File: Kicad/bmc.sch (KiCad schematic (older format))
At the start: 27 parts, among them J1101 Header, J1102 Header, J1103 Conn_01x05, J1104 Double-mini-DIN-6, SW1101 SW_DIP_x01, SW1102 SW_DIP_x01, U1101 STM32F031K6T6

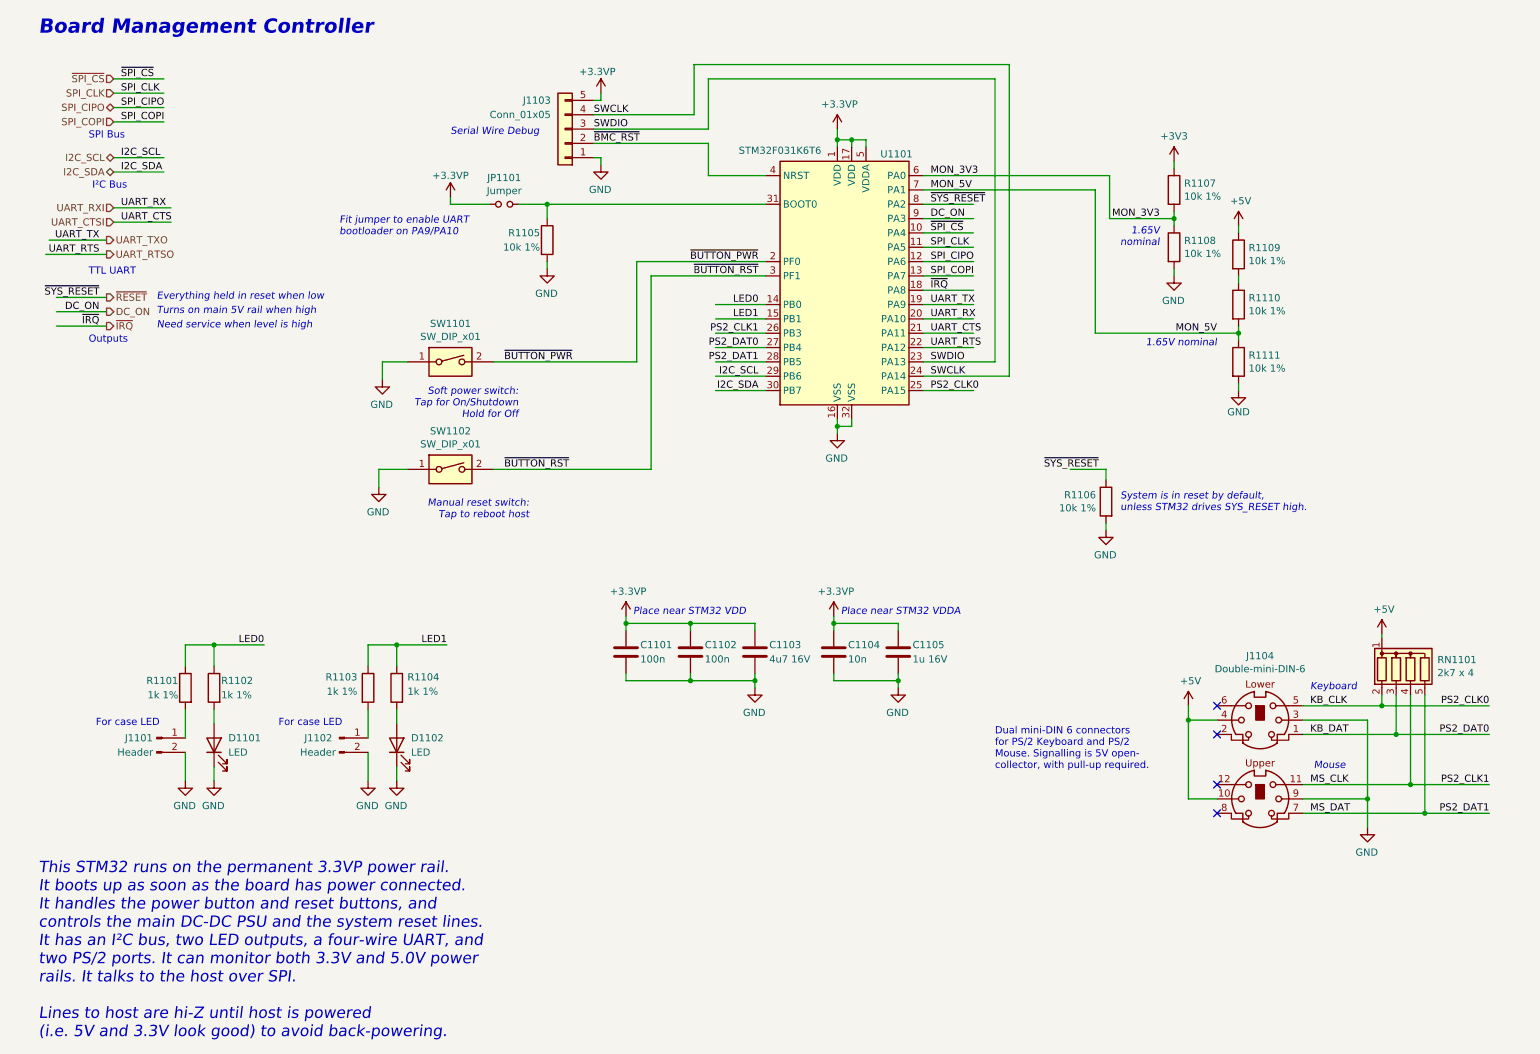
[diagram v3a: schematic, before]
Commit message: BoM and PCB fixes.
* Move tolerances and voltages out of value and into their own fields.
* Fix 5V trace for audio stage.
* Fixup docs.yml so outputs work for JLCPCB.
* Fix JLCPCB part number for 22pF caps.
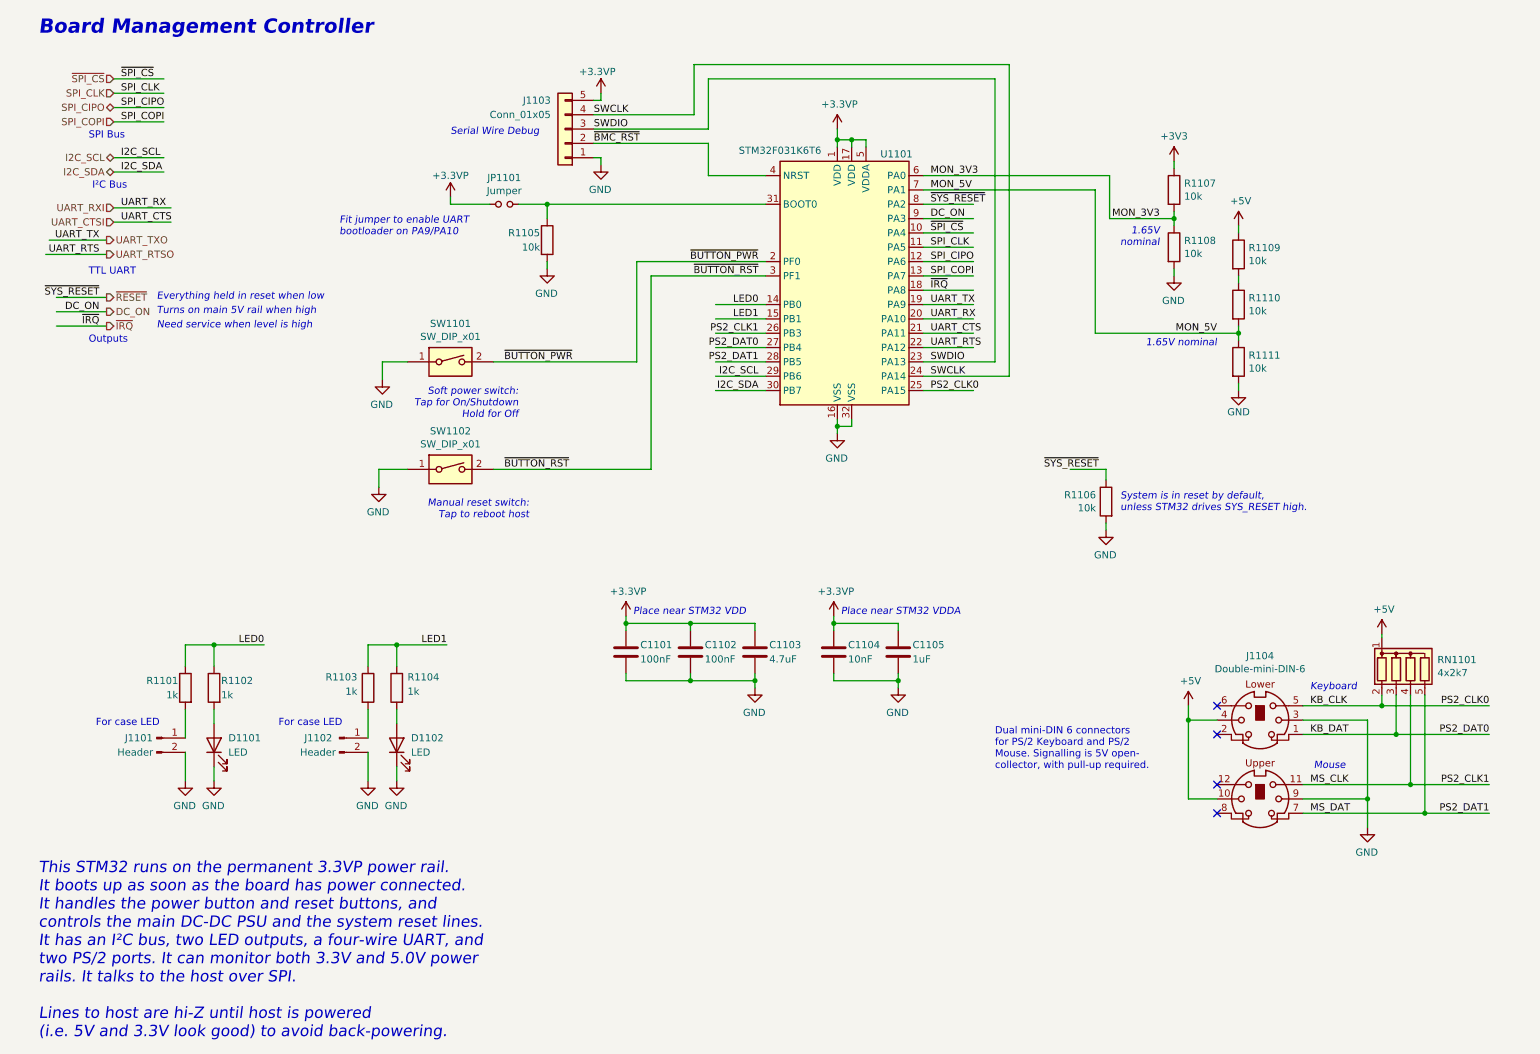
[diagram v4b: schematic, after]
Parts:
- C1101, C1102: value 100n -> 100nF
- C1103: value 4u7 16V -> 4.7uF
- C1104: value 10n -> 10nF
- C1105: value 1u 16V -> 1uF
- R1101, R1102, R1103, R1104: value 1k 1% -> 1k
- R1105, R1106, R1107, R1108, R1109, R1110, R1111: value 10k 1% -> 10k
- RN1101: value 2k7 x 4 -> 4x2k7
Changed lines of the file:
@@
 P 5550 5000
 F 0 "C1103" H 5650 5050 50  0000 L CNN
-F 1 "4u7 16V" H 5650 4950 50  0000 L CNN
+F 1 "4.7uF" H 5650 4950 50  0000 L CNN
 F 2 "Capacitor_SMD:C_0805_2012Metric_Pad1.18x1.45mm_HandSolder" H 5588 4850 50  0001 C CNN
 F 3 "~" H 5550 5000 50  0001 C CNN
@@
 P 5100 5000
 F 0 "C1102" H 5200 5050 50  0000 L CNN
-F 1 "100n" H 5200 4950 50  0000 L CNN
+F 1 "100nF" H 5200 4950 50  0000 L CNN
 F 2 "Capacitor_SMD:C_0805_2012Metric_Pad1.18x1.45mm_HandSolder" H 5138 4850 50  0001 C CNN
 F 3 "~" H 5100 5000 50  0001 C CNN
@@
 P 4650 5000
 F 0 "C1101" H 4750 5050 50  0000 L CNN
-F 1 "100n" H 4750 4950 50  0000 L CNN
+F 1 "100nF" H 4750 4950 50  0000 L CNN
 F 2 "Capacitor_SMD:C_0805_2012Metric_Pad1.18x1.45mm_HandSolder" H 4688 4850 50  0001 C CNN
 F 3 "~" H 4650 5000 50  0001 C CNN
@@
 P 4100 2125
 F 0 "R1105" H 4050 2175 50  0000 R CNN
-F 1 "10k 1%" H 4050 2075 50  0000 R CNN
+F 1 "10k" H 4050 2075 50  0000 R CNN
 F 2 "Resistor_SMD:R_0805_2012Metric_Pad1.20x1.40mm_HandSolder" V 4030 2125 50  0001 C CNN
 F 3 "~" H 4100 2125 50  0001 C CNN
@@
 P 2850 5250
 F 0 "R1103" H 2775 5325 50  0000 R CNN
-F 1 "1k 1%" H 2775 5225 50  0000 R CNN
+F 1 "1k" H 2775 5225 50  0000 R CNN
 F 2 "Resistor_SMD:R_0805_2012Metric_Pad1.20x1.40mm_HandSolder" V 2780 5250 50  0001 C CNN
 F 3 "~" H 2850 5250 50  0001 C CNN
@@
 P 3050 5250
 F 0 "R1104" H 2975 5325 50  0000 R CNN
-F 1 "1k 1%" H 2975 5225 50  0000 R CNN
+F 1 "1k" H 2975 5225 50  0000 R CNN
 F 2 "Resistor_SMD:R_0805_2012Metric_Pad1.20x1.40mm_HandSolder" V 2980 5250 50  0001 C CNN
 F 3 "~" H 3050 5250 50  0001 C CNN
@@
 P 1575 5250
 F 0 "R1101" H 1625 5300 50  0000 L CNN
-F 1 "1k 1%" H 1625 5200 50  0000 L CNN
+F 1 "1k" H 1625 5200 50  0000 L CNN
 F 2 "Resistor_SMD:R_0805_2012Metric_Pad1.20x1.40mm_HandSolder" V 1505 5250 50  0001 C CNN
 F 3 "~" H 1575 5250 50  0001 C CNN
@@
 P 1775 5250
 F 0 "R1102" H 1725 5300 50  0000 R CNN
-F 1 "1k 1%" H 1725 5200 50  0000 R CNN
+F 1 "1k" H 1725 5200 50  0000 R CNN
 F 2 "Resistor_SMD:R_0805_2012Metric_Pad1.20x1.40mm_HandSolder" V 1705 5250 50  0001 C CNN
 F 3 "~" H 1775 5250 50  0001 C CNN
@@
 P 10125 5100
 F 0 "RN1101" H 10313 5146 50  0000 L CNN
-F 1 "2k7 x 4" H 10313 5055 50  0000 L CNN
+F 1 "4x2k7" H 10313 5055 50  0000 L CNN
 F 2 "Resistor_THT:R_Array_SIP5" V 10400 5100 50  0001 C CNN
 F 3 "http://www.vishay.com/docs/31509/csc.pdf" H 10125 5100 50  0001 C CNN
@@
 P 6550 5000
 F 0 "C1105" H 6650 5050 50  0000 L CNN
-F 1 "1u 16V" H 6650 4950 50  0000 L CNN
+F 1 "1uF" H 6650 4950 50  0000 L CNN
 F 2 "Capacitor_SMD:C_0805_2012Metric_Pad1.18x1.45mm_HandSolder" H 6588 4850 50  0001 C CNN
 F 3 "~" H 6550 5000 50  0001 C CNN
@@
 P 6100 5000
 F 0 "C1104" H 6200 5050 50  0000 L CNN
-F 1 "10n" H 6200 4950 50  0000 L CNN
+F 1 "10nF" H 6200 4950 50  0000 L CNN
 F 2 "Capacitor_SMD:C_0805_2012Metric_Pad1.18x1.45mm_HandSolder" H 6138 4850 50  0001 C CNN
 F 3 "~" H 6100 5000 50  0001 C CNN
@@
 P 8925 2975
 F 0 "R1111" H 8995 3021 50  0000 L CNN
-F 1 "10k 1%" H 8995 2930 50  0000 L CNN
+F 1 "10k" H 8995 2930 50  0000 L CNN
 F 2 "Resistor_SMD:R_0805_2012Metric_Pad1.20x1.40mm_HandSolder" V 8855 2975 50  0001 C CNN
 F 3 "~" H 8925 2975 50  0001 C CNN
@@
 P 8925 2575
 F 0 "R1110" H 8995 2621 50  0000 L CNN
-F 1 "10k 1%" H 8995 2530 50  0000 L CNN
+F 1 "10k" H 8995 2530 50  0000 L CNN
 F 2 "Resistor_SMD:R_0805_2012Metric_Pad1.20x1.40mm_HandSolder" V 8855 2575 50  0001 C CNN
 F 3 "~" H 8925 2575 50  0001 C CNN
@@
 P 8925 2225
 F 0 "R1109" H 8995 2271 50  0000 L CNN
-F 1 "10k 1%" H 8995 2180 50  0000 L CNN
+F 1 "10k" H 8995 2180 50  0000 L CNN
 F 2 "Resistor_SMD:R_0805_2012Metric_Pad1.20x1.40mm_HandSolder" V 8855 2225 50  0001 C CNN
 F 3 "~" H 8925 2225 50  0001 C CNN
@@
 P 8475 2175
 F 0 "R1108" H 8545 2221 50  0000 L CNN
-F 1 "10k 1%" H 8545 2130 50  0000 L CNN
+F 1 "10k" H 8545 2130 50  0000 L CNN
 F 2 "Resistor_SMD:R_0805_2012Metric_Pad1.20x1.40mm_HandSolder" V 8405 2175 50  0001 C CNN
 F 3 "~" H 8475 2175 50  0001 C CNN
@@
 P 8475 1775
 F 0 "R1107" H 8545 1821 50  0000 L CNN
-F 1 "10k 1%" H 8545 1730 50  0000 L CNN
+F 1 "10k" H 8545 1730 50  0000 L CNN
 F 2 "Resistor_SMD:R_0805_2012Metric_Pad1.20x1.40mm_HandSolder" V 8405 1775 50  0001 C CNN
 F 3 "~" H 8475 1775 50  0001 C CNN
@@
 P 8000 3950
 F 0 "R1106" H 8070 3996 50  0000 L CNN
-F 1 "10k 1%" H 8070 3905 50  0000 L CNN
+F 1 "10k" H 8070 3905 50  0000 L CNN
 F 2 "Resistor_SMD:R_0805_2012Metric_Pad1.20x1.40mm_HandSolder" V 7930 3950 50  0001 C CNN
 F 3 "~" H 8000 3950 50  0001 C CNN

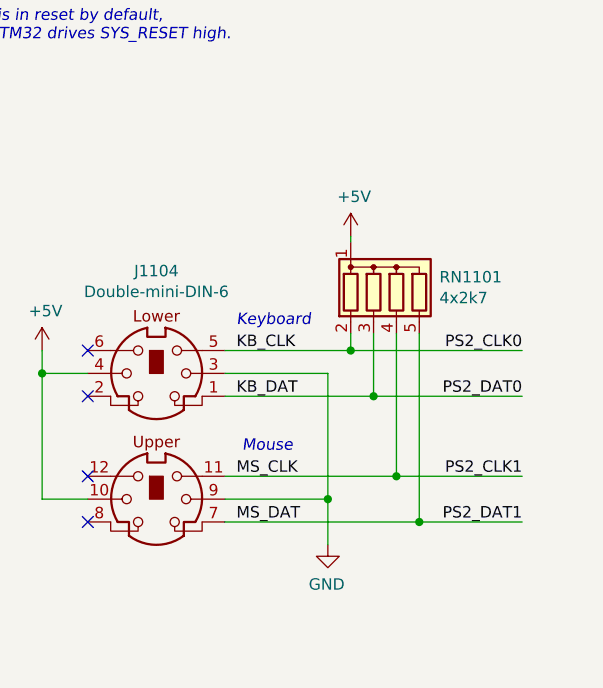
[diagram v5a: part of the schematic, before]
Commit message: Remove PS/2 SIP array and fix DC jack value. (#26)
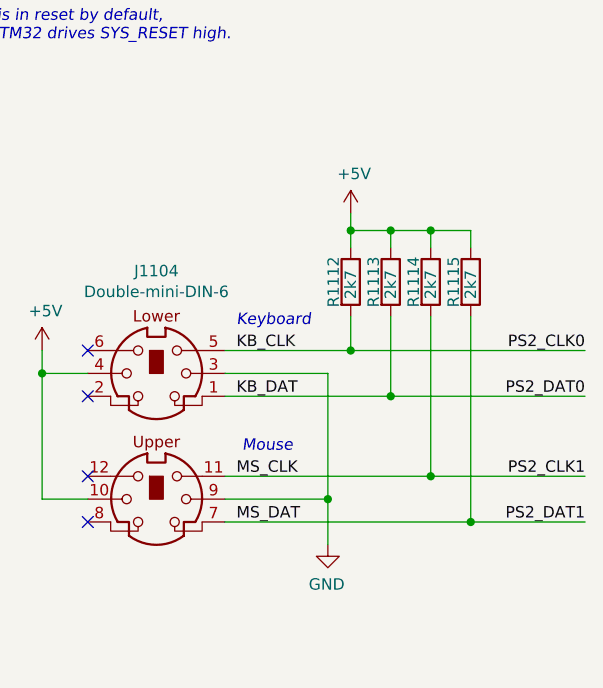
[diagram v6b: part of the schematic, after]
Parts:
- removed RN1101: 4x2k7, Resistor_THT:R_Array_SIP5, symbol Device:R_Network04
- added R1112, R1113, R1114, R1115: 2k7, Resistor_SMD:R_0805_2012Metric_Pad1.20x1.40mm_HandSolder, symbol Device:R
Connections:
- wire segments 150 -> 157
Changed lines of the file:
@@
 	1    0    0    -1
 $EndComp
-Text Label 10675 5375 2    50   ~ 0
+Text Label 10950 5375 2    50   ~ 0
 PS2_CLK0
-Text Label 10675 5575 2    50   ~ 0
+Text Label 10950 5575 2    50   ~ 0
 PS2_DAT0
-Text Label 10675 5925 2    50   ~ 0
+Text Label 10950 5925 2    50   ~ 0
 PS2_CLK1
-Text Label 10675 6125 2    50   ~ 0
+Text Label 10950 6125 2    50   ~ 0
 PS2_DAT1
 Text Notes 9425 5275 0    50   Italic 0
@@
 Mouse
 Wire Wire Line
-	9925 5375 9925 5300
-Wire Wire Line
 	9375 5375 9925 5375
 Wire Wire Line
-	10025 5575 10025 5300
-Wire Wire Line
-	9375 5575 10025 5575
-Wire Wire Line
-	10125 5925 10125 5300
-Wire Wire Line
-	9375 5925 10125 5925
-Wire Wire Line
-	10225 6125 10225 5300
-Wire Wire Line
-	9375 6125 10225 6125
+	9375 5575 10100 5575
+Wire Wire Line
+	9375 5925 10275 5925
+Wire Wire Line
+	9375 6125 10450 6125
 $Comp
 L power:+5V #PWR01124
 U 1 1 6031C569
-P 9925 4875
-F 0 "#PWR01124" H 9925 4725 50  0001 C CNN
-F 1 "+5V" H 9940 5048 50  0000 C CNN
-F 2 "" H 9925 4875 50  0001 C CNN
-F 3 "" H 9925 4875 50  0001 C CNN
-	1    9925 4875
-	1    0    0    -1
-$EndComp
-Wire Wire Line
-	9925 4875 9925 4900
+P 9925 4775
+F 0 "#PWR01124" H 9925 4625 50  0001 C CNN
+F 1 "+5V" H 9940 4948 50  0000 C CNN
+F 2 "" H 9925 4775 50  0001 C CNN
+F 3 "" H 9925 4775 50  0001 C CNN
+	1    9925 4775
+	1    0    0    -1
+$EndComp
 Text Label 5575 2875 2    50   ~ 0
 PS2_DAT0
@@
 	3425 1875 3700 1875
 Wire Wire Line
-	9925 5375 10675 5375
+	9925 5375 10950 5375
 Connection ~ 9925 5375
 Wire Wire Line
-	10025 5575 10675 5575
-Connection ~ 10025 5575
-Wire Wire Line
-	10125 5925 10675 5925
-Connection ~ 10125 5925
-Wire Wire Line
-	10225 6125 10675 6125
-Connection ~ 10225 6125
+	10100 5575 10950 5575
+Connection ~ 10100 5575
+Wire Wire Line
+	10275 5925 10950 5925
+Connection ~ 10275 5925
+Wire Wire Line
+	10450 6125 10950 6125
+Connection ~ 10450 6125
 Text Label 9425 5375 0    50   ~ 0
 KB_CLK
@@
 	1    0    0    -1
 $EndComp
-$Comp
-L Device:R_Network04 RN1101
-U 1 1 60303C59
-P 10125 5100
-F 0 "RN1101" H 10313 5146 50  0000 L CNN
-F 1 "4x2k7" H 10313 5055 50  0000 L CNN
-F 2 "Resistor_THT:R_Array_SIP5" V 10400 5100 50  0001 C CNN
-F 3 "http://www.vishay.com/docs/31509/csc.pdf" H 10125 5100 50  0001 C CNN
-F 4 "0" H 10125 5100 50  0001 C CNN "DNP"
-F 5 "4605X-101-272LF-ND" H 10125 5100 50  0001 C CNN "Digikey"
-F 6 "4605X-101-272LF" H 10125 5100 50  0001 C CNN "MPN"
-F 7 "Bourns" H 10125 5100 50  0001 C CNN "Manufacturer"
-F 8 "652-4605X-1LF-2.7K" H 10125 5100 50  0001 C CNN "Mouser"
-F 9 "~" H 10125 5100 50  0001 C CNN "LCSC Part#"
-	1    10125 5100
-	1    0    0    -1
-$EndComp
 Wire Wire Line
 	4725 2975 4725 2275
@@
 Text Notes 550  7700 0    79   Italic 0
 This STM32 runs on the permanent 3.3VP power rail.\nIt boots up as soon as the board has power connected.\nIt handles the power button and reset buttons, and\ncontrols the main DC-DC PSU and the system reset lines.\nIt has an I²C bus, two LED outputs, a four-wire UART, and\ntwo PS/2 ports. It can monitor both 3.3V and 5.0V power\nrails. It talks to the host over SPI.\n\nLines to host are hi-Z until host is powered\n(i.e. 5V and 3.3V look good) to avoid back-powering.
+$Comp
+L Device:R R1114
+U 1 1 60CD12AF
+P 10275 5075
+F 0 "R1114" V 10200 5075 50  0000 C CNN
+F 1 "2k7" V 10275 5000 50  0000 L CNN
+F 2 "Resistor_SMD:R_0805_2012Metric_Pad1.20x1.40mm_HandSolder" V 10205 5075 50  0001 C CNN
+F 3 "~" H 10275 5075 50  0001 C CNN
+	1    10275 5075
+	1    0    0    -1
+$EndComp
+$Comp
+L Device:R R1115
+U 1 1 60CD16F7
+P 10450 5075
+F 0 "R1115" V 10375 5075 50  0000 C CNN
+F 1 "2k7" V 10450 5000 50  0000 L CNN
+F 2 "Resistor_SMD:R_0805_2012Metric_Pad1.20x1.40mm_HandSolder" V 10380 5075 50  0001 C CNN
+F 3 "~" H 10450 5075 50  0001 C CNN
+	1    10450 5075
+	1    0    0    -1
+$EndComp
+Wire Wire Line
+	9925 4850 10100 4850
+Wire Wire Line
+	10450 4850 10450 4925
+Wire Wire Line
+	9925 4775 9925 4850
+Wire Wire Line
+	10275 4925 10275 4850
+Connection ~ 10275 4850
+Wire Wire Line
+	10275 4850 10450 4850
+Wire Wire Line
+	10100 4925 10100 4850
+Connection ~ 10100 4850
+Wire Wire Line
+	10100 4850 10275 4850
+Wire Wire Line
+	9925 4925 9925 4850
+Connection ~ 9925 4850
+$Comp
+L Device:R R1113
+U 1 1 60CD0A39
+P 10100 5075
+F 0 "R1113" V 10025 5075 50  0000 C CNN
+F 1 "2k7" V 10100 5000 50  0000 L CNN
+F 2 "Resistor_SMD:R_0805_2012Metric_Pad1.20x1.40mm_HandSolder" V 10030 5075 50  0001 C CNN
+F 3 "~" H 10100 5075 50  0001 C CNN
+	1    10100 5075
+	1    0    0    -1
+$EndComp
+$Comp
+L Device:R R1112
+U 1 1 60C73816
+P 9925 5075
+F 0 "R1112" V 9850 5075 50  0000 C CNN
+F 1 "2k7" V 9925 5000 50  0000 L CNN
+F 2 "Resistor_SMD:R_0805_2012Metric_Pad1.20x1.40mm_HandSolder" V 9855 5075 50  0001 C CNN
+F 3 "~" H 9925 5075 50  0001 C CNN
+	1    9925 5075
+	1    0    0    -1
+$EndComp
+Wire Wire Line
+	9925 5225 9925 5375
+Wire Wire Line
+	10100 5225 10100 5575
+Wire Wire Line
+	10275 5225 10275 5925
+Wire Wire Line
+	10450 5225 10450 6125
 $EndSCHEMATC

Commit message: Update component values.
Tolerance and Voltage are set to the minimum acceptable. The selected
parts can be better, where a better part is cheaper or has
better availability.

Also dropped R2R DAC tolerance to 1% - 0.5% was overkill. The output
resistor had the wrong value too, which is fixed.
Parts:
- C1101, C1102, C1103, C1104, C1105: Tolerance (none) -> X5R; Voltage (none) -> 10V
- D1101, D1102: Digikey 732-5006-ND -> (none); Mouser 151031SS06000 -> (none)
- R1101, R1102, R1103, R1104, R1105, R1106, R1107, R1108, R1109, R1110, R1111: Tolerance (none) -> 1%
- R1112, R1113, R1114, R1115: value 2k7 -> 1k; DNP (none) -> 0; LCSC Part# (none) -> C17513; MPN (none) -> CPL-RES-0805-1K-0.125W; Manufacturer (none) -> CPL; Tolerance (none) -> 1%
